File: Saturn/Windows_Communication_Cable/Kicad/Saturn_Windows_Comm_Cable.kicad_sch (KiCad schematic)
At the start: 8 parts, among them J1 SegaSaturn, J2 Windows_RS232

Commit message: Updates
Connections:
- net GND: now also C7.1, J1.12 (Pin_12), J1.8 (Pin_8), J2.7; no longer C7.2, J2.1
- net SATURN_RED: now also U1.11 (R_{CON}), U1.12 (R_{IN2}), U1.16 (D_{CON})
- net at U1.3 (V_{CC}): now also C7.2; no longer C7.1
- no-connect marks 3 -> 10
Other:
- company: (none) -> ASCII Corp.
- moved on the sheet: C1, C2, C4, C7

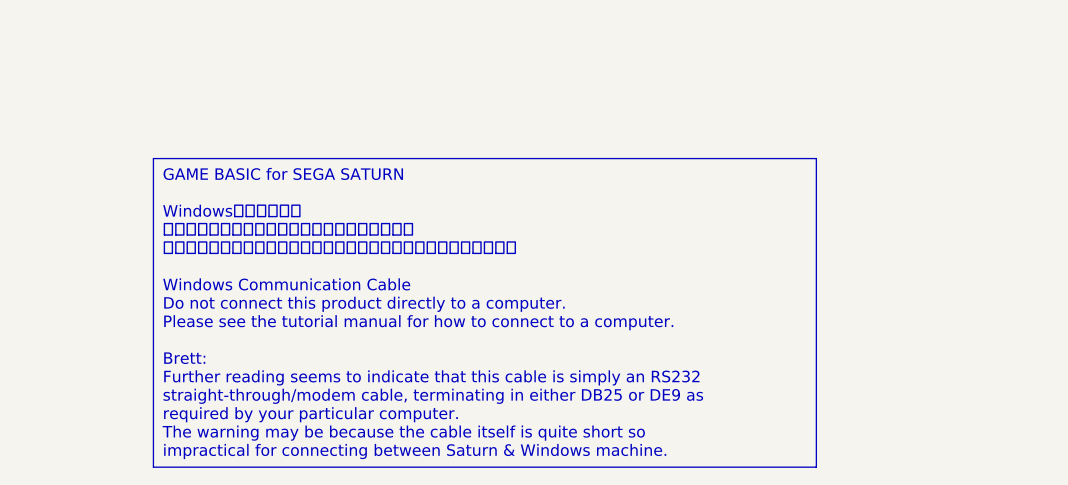
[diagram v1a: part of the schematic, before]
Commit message: Redesign PCB shape
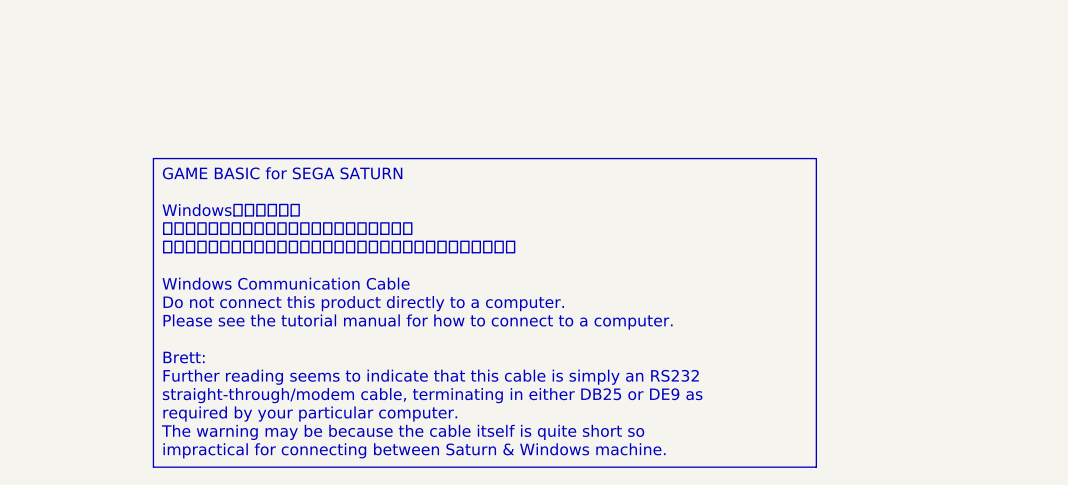
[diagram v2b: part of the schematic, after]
